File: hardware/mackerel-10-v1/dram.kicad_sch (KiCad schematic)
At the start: 9 parts, among them J4 Conn_01x10, J5 Conn_02x05_Odd_Even

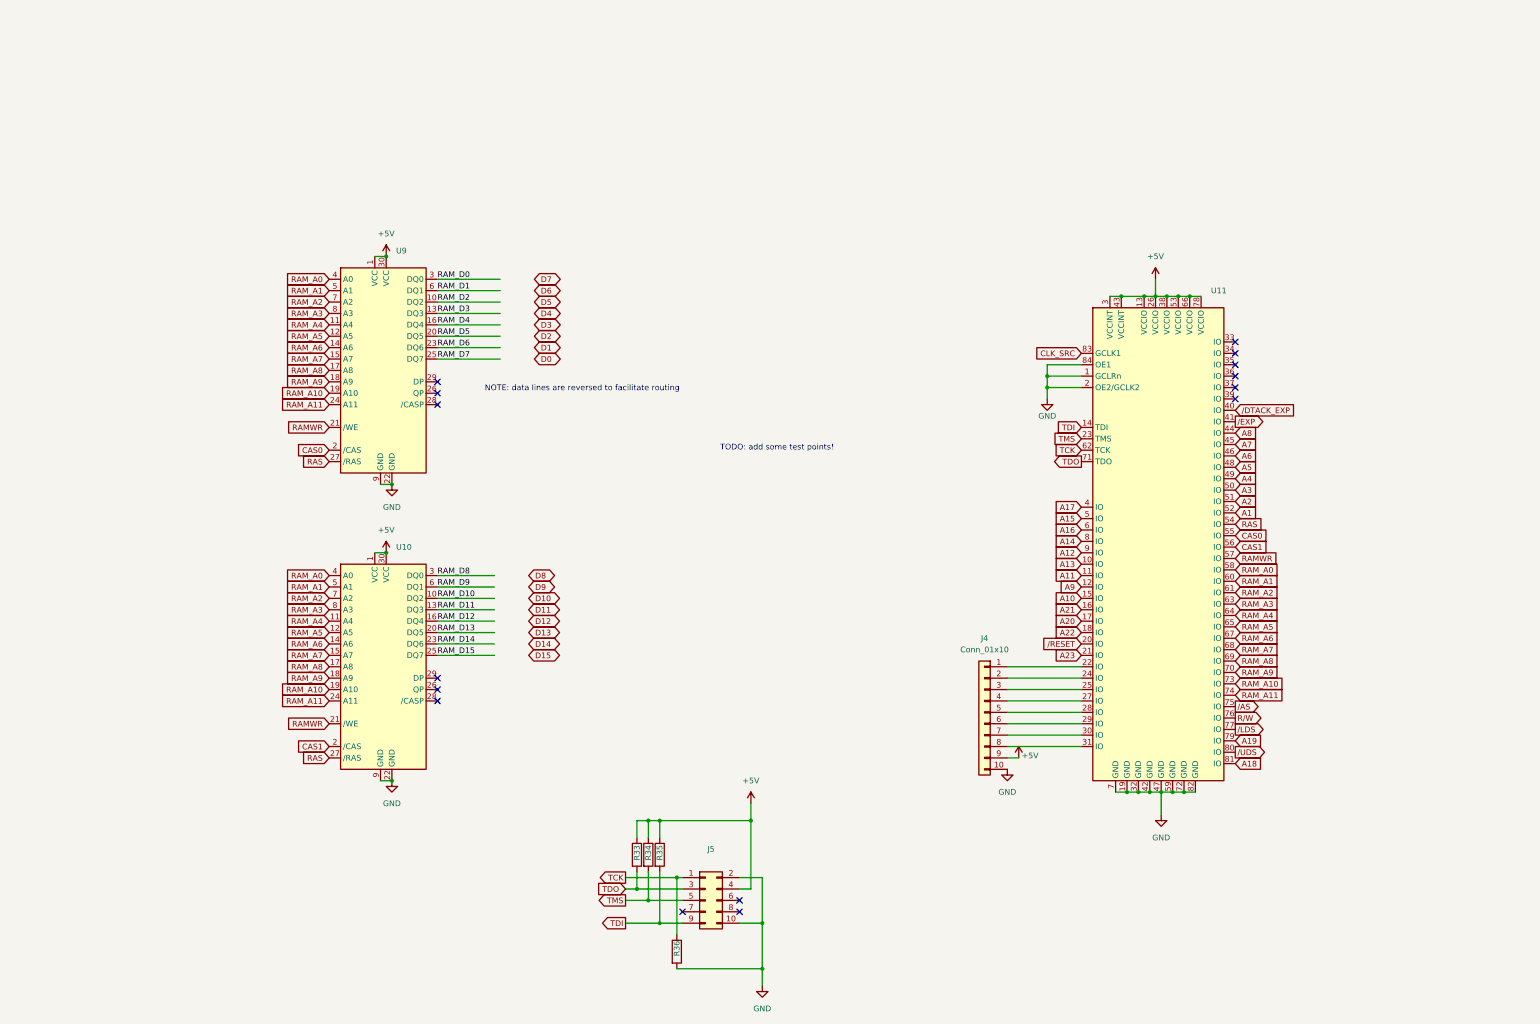
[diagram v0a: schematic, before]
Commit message: Rough layout of components on PCB
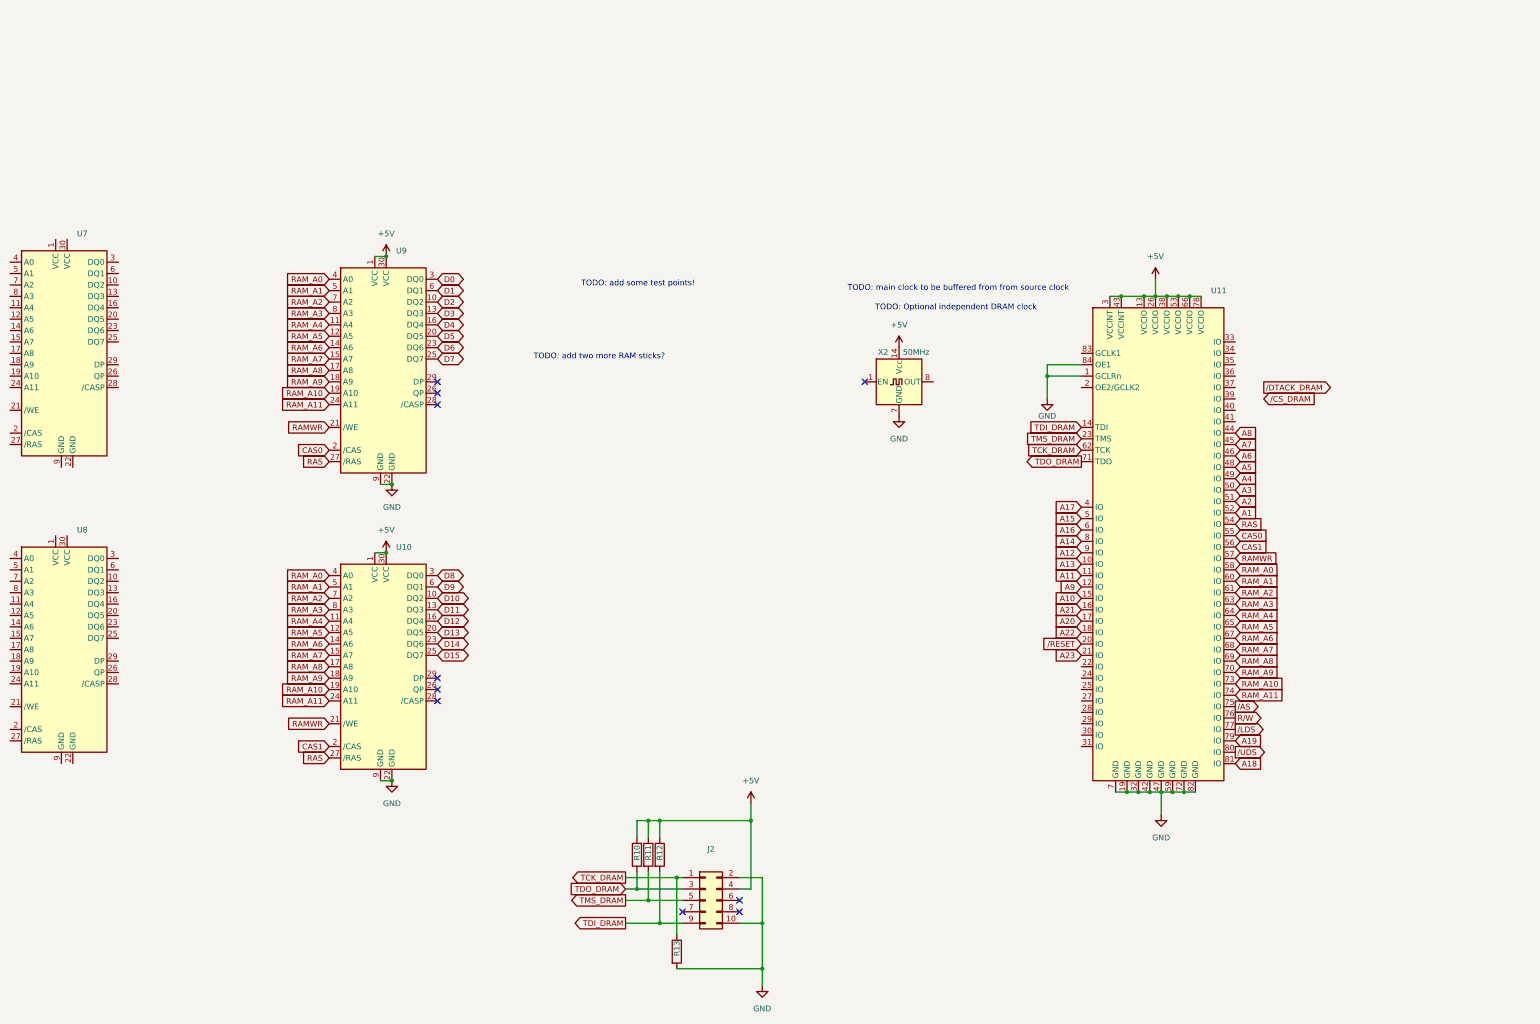
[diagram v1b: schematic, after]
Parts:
- removed J4: Conn_01x10, Connector_PinSocket_2.54mm:PinSocket_1x10_P2.54mm_Vertical, symbol Connector_Generic:Conn_01x10
- added U7, U8: ~, mackerel:SIMM-30, symbol mackerel-68k-symbols:SIMM30
- added X2: 50MHz, Oscillator:Oscillator_DIP-14, symbol Oscillator:CXO_DIP14
- renumbered J5 to J2, R33 to R10, R34 to R11, R35 to R12, R36 to R13
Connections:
- net RAM_D0 is gone; now on net D0: U9.3 (DQ0)
- net RAM_D1 is gone; now on net D1: U9.6 (DQ1)
- net RAM_D10 is gone; now on net D10: U10.10 (DQ2)
- net RAM_D11 is gone; now on net D11: U10.13 (DQ3)
- net RAM_D12 is gone; now on net D12: U10.16 (DQ4)
- net RAM_D13 is gone; now on net D13: U10.20 (DQ5)
- net RAM_D14 is gone; now on net D14: U10.23 (DQ6)
- net RAM_D15 is gone; now on net D15: U10.25 (DQ7)
- net RAM_D2 is gone; now on net D2: U9.10 (DQ2)
- net RAM_D3 is gone; now on net D3: U9.13 (DQ3)
- net RAM_D4 is gone; now on net D4: U9.16 (DQ4)
- net RAM_D5 is gone; now on net D5: U9.20 (DQ5)
- net RAM_D6 is gone; now on net D6: U9.23 (DQ6)
- net RAM_D7 is gone; now on net D7: U9.25 (DQ7)
- net RAM_D8 is gone; now on net D8: U10.3 (DQ0)
- net RAM_D9 is gone; now on net D9: U10.6 (DQ1)
- net +5V: now also X2.14 (Vcc)
- net GND: now also X2.7 (GND); no longer U11.2 (OE2/GCLK2)
- net CLK_SRC: no longer names the net of U11.83 (GCLK1)
- net TCK renamed TCK_DRAM
- net TDI renamed TDI_DRAM
- net TDO renamed TDO_DRAM
- net TMS renamed TMS_DRAM
- net /DTACK_EXP: no longer names the net of U11.40 (IO)
- net /EXP: no longer names the net of U11.41 (IO)
- no-connect marks 15 -> 10
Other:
- note added: "TODO: Optional independent DRAM clock"
- note added: "TODO: add two more RAM sticks?"
- note added: "TODO: main clock to be buffered from from source clock"
- note removed: "NOTE: data lines are reversed to facilitate routing"

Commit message: Settled on mini ITX form factor
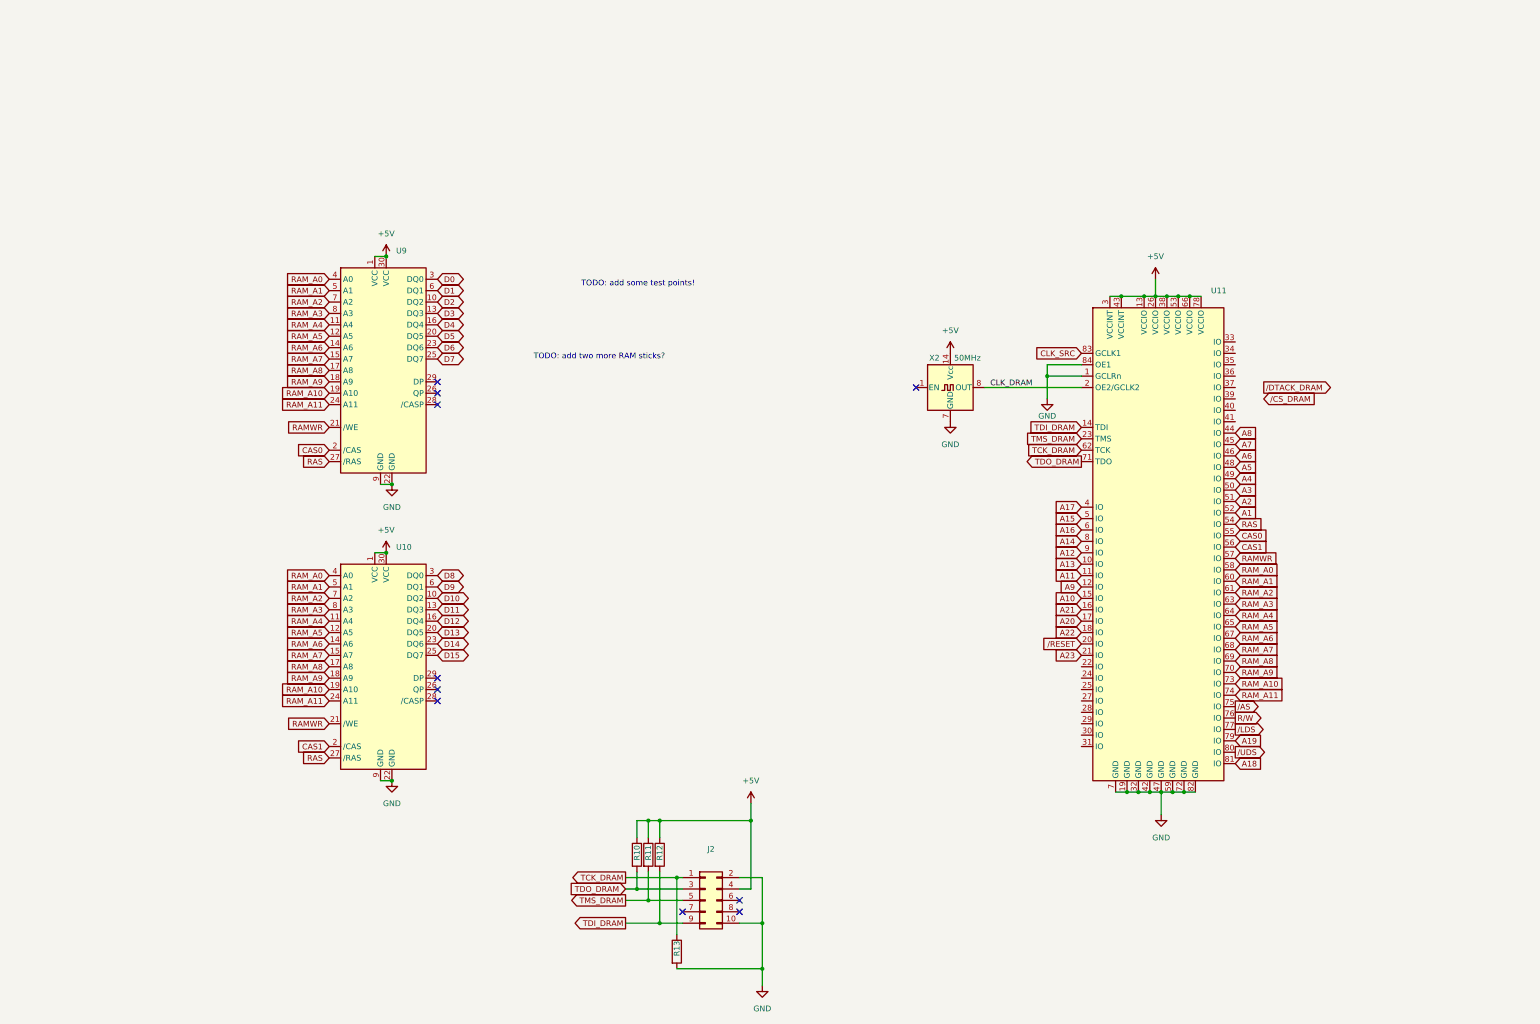
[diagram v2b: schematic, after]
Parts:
- removed U7, U8: ~, mackerel:SIMM-30, symbol mackerel-68k-symbols:SIMM30
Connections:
- net CLK_DRAM: now reaches X2.8 (OUT)
- net CLK_DRAM: now also U11.2 (OE2/GCLK2)
- net CLK_SRC: now reaches U11.83 (GCLK1)
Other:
- note removed: "TODO: Optional independent DRAM clock"
- note removed: "TODO: main clock to be buffered from from source clock"
- moved on the sheet: X2

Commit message: Another layout plan
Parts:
- removed X2: 50MHz, Oscillator:Oscillator_DIP-14, symbol Oscillator:CXO_DIP14
- added C1, C2, C3, C4: 470uF, Capacitor_THT:CP_Radial_D8.0mm_P3.50mm, symbol Device:C_Polarized_US
- added C10, C11, C12, C13, C14, C15, C5, C6: C, Capacitor_THT:C_Disc_D4.3mm_W1.9mm_P5.00mm, symbol Device:C
- added U7, U8: ~, mackerel:SIMM-30, symbol mackerel-68k-symbols:SIMM30
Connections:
- net +5V: now also C1.1, C10.1, C11.1, C12.2, C13.2, C14.2, C15.2, C2.1, C3.1, C4.1, C5.1, C6.1, U7.1 (VCC), U7.30 (VCC), U8.1 (VCC), U8.30 (VCC)
- net CAS0: no longer U11.55 (IO), U9.2 (/CAS)
- net CAS1: no longer U10.2 (/CAS), U11.56 (IO)
- net D0: now also U7.3 (DQ0)
- net D1: now also U7.6 (DQ1)
- net D10: now also U8.10 (DQ2)
- net D11: now also U8.13 (DQ3)
- net D12: now also U8.16 (DQ4)
- net D13: now also U8.20 (DQ5)
- net D14: now also U8.23 (DQ6)
- net D15: now also U8.25 (DQ7)
- net D2: now also U7.10 (DQ2)
- net D3: now also U7.13 (DQ3)
- net D4: now also U7.16 (DQ4)
- net D5: now also U7.20 (DQ5)
- net D6: now also U7.23 (DQ6)
- net D7: now also U7.25 (DQ7)
- net D8: now also U8.3 (DQ0)
- net D9: now also U8.6 (DQ1)
- net GND: now also C1.2, C10.2, C11.2, C12.1, C13.1, C14.1, C15.1, C2.2, C3.2, C4.2, C5.2, C6.2, U7.22 (GND), U7.9 (GND), U8.22 (GND), U8.9 (GND)
- net RAMWR: no longer U10.21 (/WE), U11.57 (IO), U9.21 (/WE)
- net RAM_A0: now also U7.4 (A0), U8.4 (A0)
- net RAM_A1: now also U7.5 (A1), U8.5 (A1)
- net RAM_A10: now also U7.19 (A10), U8.19 (A10)
- net RAM_A11: now also U7.24 (A11), U8.24 (A11)
- net RAM_A2: now also U7.7 (A2), U8.7 (A2)
- net RAM_A3: now also U7.8 (A3), U8.8 (A3)
- net RAM_A4: now also U7.11 (A4), U8.11 (A4)
- net RAM_A5: now also U7.12 (A5), U8.12 (A5)
- net RAM_A6: now also U7.14 (A6), U8.14 (A6)
- net RAM_A7: now also U7.15 (A7), U8.15 (A7)
- net RAM_A8: now also U7.17 (A8), U8.17 (A8)
- net RAM_A9: now also U7.18 (A9), U8.18 (A9)
- net RAS: no longer U10.27 (/RAS), U11.54 (IO), U9.27 (/RAS)
- net CLK_DRAM: no longer names the net of U11.2 (OE2/GCLK2)
- new net CASA0: U9.2 (/CAS)
- new net CASA1: U10.2 (/CAS)
- new net CASB0: U7.2 (/CAS)
- new net CASB1: U8.2 (/CAS)
- new net RAMWRA: U10.21 (/WE), U9.21 (/WE)
- new net RAMWRB: U7.21 (/WE), U8.21 (/WE)
- new net RASA: U10.27 (/RAS), U9.27 (/RAS)
- new net RASB: U7.27 (/RAS), U8.27 (/RAS)
- no-connect marks 10 -> 15

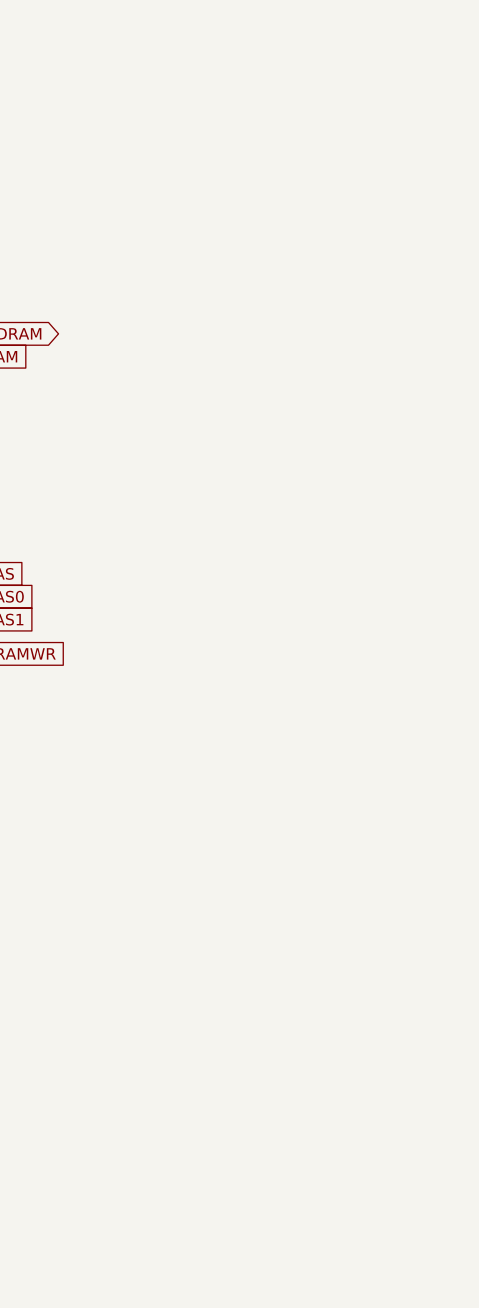
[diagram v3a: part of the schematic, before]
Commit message: half routed
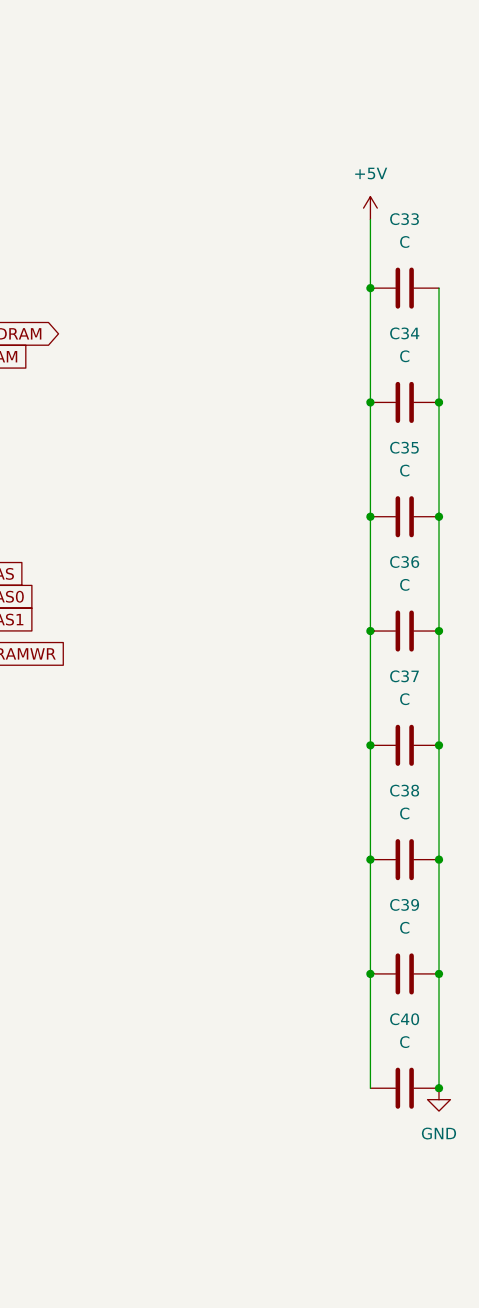
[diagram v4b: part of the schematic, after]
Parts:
- added C33, C34, C35, C36, C37, C38, C39, C40: C, Capacitor_THT:C_Disc_D4.3mm_W1.9mm_P5.00mm, symbol Device:C
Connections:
- net +5V: now also C33.1, C34.1, C35.1, C36.1, C37.2, C38.2, C39.2, C40.2
- net GND: now also C33.2, C34.2, C35.2, C36.2, C37.1, C38.1, C39.1, C40.1
